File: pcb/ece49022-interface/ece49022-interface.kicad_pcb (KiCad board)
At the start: 4 copper layers, 60.2 x 52.2 mm, 37 parts, among them J1 Conn_01x04_Pin, J2 Conn_01x05_Pin, J3 Conn_01x04_Pin, J4 Conn_01x04_Pin, J5 Conn_01x08_Pin, J6 Conn_01x02_Pin, Q1 KSC1815, U2 TPS54202DDCT

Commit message: added stuff
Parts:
- added J7: Conn_01x04_Pin, Connector_PinHeader_2.54mm:PinHeader_1x04_P2.54mm_Vertical, F.Cu at (137.9, 120.8)
- added J8: Conn_01x04_Pin, Connector_PinHeader_2.54mm:PinHeader_1x04_P2.54mm_Vertical, F.Cu at (137.9, 116.9)
- J5: value Conn_01x08_Pin -> Conn_01x04_Pin; footprint Connector_PinHeader_2.54mm:PinHeader_1x08_P2.54mm_Vertical -> Connector_PinHeader_2.54mm:PinHeader_1x04_P2.54mm_Vertical
- moved J5 15.2 mm to (137.9, 113.0), turned to -90 degrees
- moved H3 12.8 mm to (131.1, 107.4)
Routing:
- net /MAIN_MCU_I2C_SDA: track 36.6 -> 17.6 mm
- net +5V: track 30.2 -> 13.2 mm
- net /MAIN_MCU_I2C_SCL: track 33.8 -> 18.2 mm

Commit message: no warnings
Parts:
- moved Buzzer1 6.68 mm to (141.2, 91.5)
- moved C9 6.68 mm to (183.1, 97.6)
- moved D1 6.68 mm to (180.7, 72.0)
- moved H2 6.68 mm to (189.9, 70.5)
- moved L2 6.68 mm to (181.5, 103.6)
- moved Q1 6.68 mm to (142.9, 100.5)
- moved R1 6.68 mm to (180.9, 85.2)
- moved R10 6.68 mm to (180.9, 96.4)
- moved R14 6.68 mm to (182.9, 92.9)
- moved R5 6.68 mm to (142.2, 77.0)
- moved R9 6.68 mm to (180.9, 94.3)
- moved H4 6.68 mm to (189.8, 116.3)
- moved J1 6.68 mm to (190.8, 81.0)
- moved J6 6.68 mm to (190.8, 92.5)
- moved MOSFET1 6.68 mm to (183.5, 85.3)
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
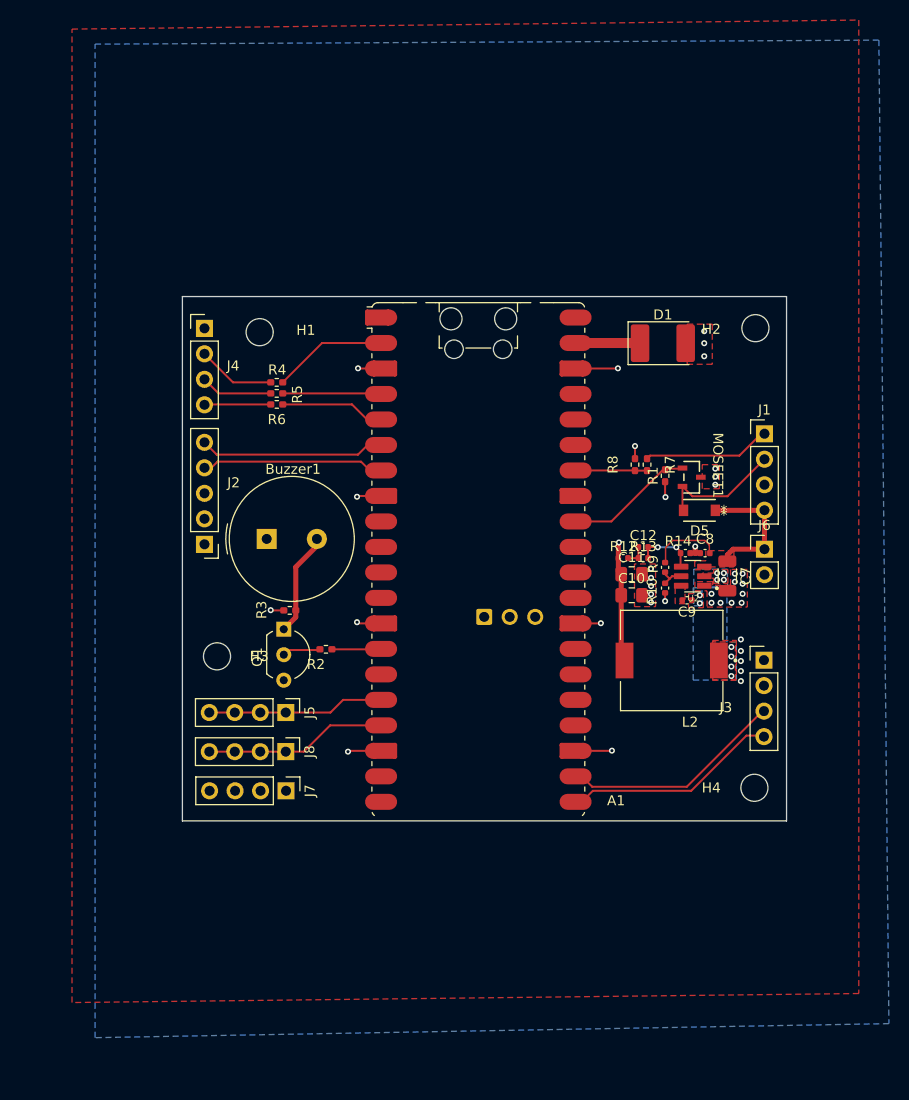
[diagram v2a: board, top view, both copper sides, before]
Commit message: Added cutout
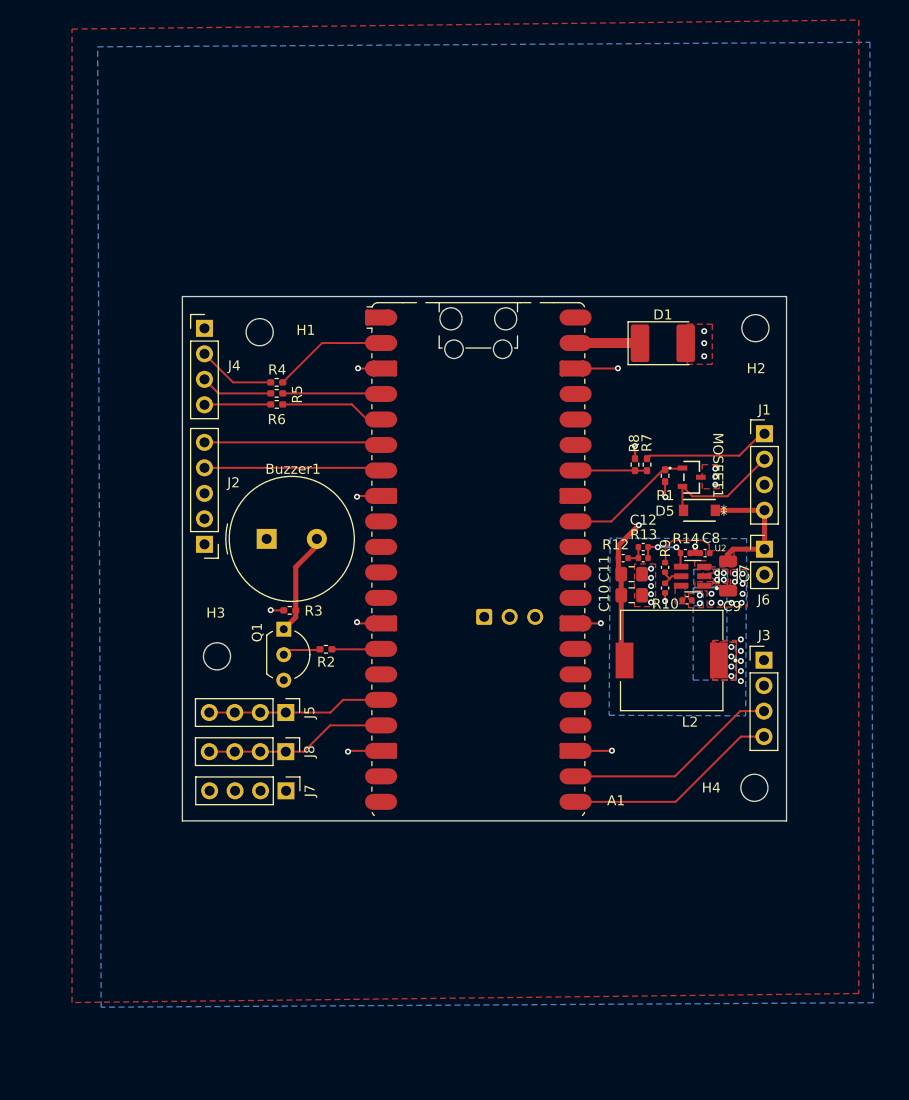
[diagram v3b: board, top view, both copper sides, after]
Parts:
- moved C7 0.08 mm to (187.2, 95.2)
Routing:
- net +5V: track 13.2 -> 15.9 mm
- net /BC_Rx: track 19.1 -> 17.7 mm
- net /BC_Tx: track 18.8 -> 17.7 mm
- net /FS_Rx: track 20.8 -> 21.5 mm
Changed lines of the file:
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@@
 		(tags "capacitor")
 		(property "Reference" "C8"
-			(at 0 1.4 0)
+			(at -0.595 1.492378 0)
 			(layer "F.SilkS")
 			(effects
@@
 		(tags "resistor handsolder")
 		(property "Reference" "R3"
-			(at 2.8025 0.05 90)
+			(at -2.375 -0.0525 0)
 			(layer "F.SilkS")
 			(effects
@@
 		(tags "SMF5V0A-E3-08 ")
 		(property "Reference" "D5"
-			(at -0.011901 -2.0356 0)
+			(at 3.449401 -0.071251 0)
 			(unlocked yes)
 			(layer "F.SilkS")
@@
 		(tags "resistor handsolder")
 		(property "Reference" "R7"
-			(at 0.005 -2.3 90)
+			(at -2.1775 0.025 90)
 			(layer "F.SilkS")
 			(effects
@@
 		(tags "capacitor")
 		(property "Reference" "R10"
-			(at 0.32 1.3 90)
+			(at 1.577622 -0.025 180)
 			(layer "F.SilkS")
 			(effects
@@
 		(tags "Through hole pin header THT 1x02 2.54mm single row")
 		(property "Reference" "J6"
-			(at 0 -2.38 0)
+			(at -0.075 5.05 0)
 			(layer "F.SilkS")
 			(effects
@@
 		(tags "resistor handsolder")
 		(property "Reference" "R8"
-			(at 0 -2.2 90)
+			(at 2.125 -0.075 90)
 			(layer "F.SilkS")
 			(effects
@@
 		(tags "capacitor")
 		(property "Reference" "R9"
-			(at -0.32 1.2 90)
+			(at -1.912378 -0.025 90)
 			(layer "F.SilkS")
 			(effects
@@
 		(tags "TO-92L Inline Wide transistor")
 		(property "Reference" "Q1"
-			(at 2.775 2.65 90)
+			(at 0.3275 2.65 90)
 			(layer "F.SilkS")
 			(effects
@@
 		(at 183.63 95.192378 180)
 		(property "Reference" "U2"
-			(at -0.068 -2.2064 0)
+			(at -2.77 2.792378 0)
 			(layer "F.SilkS")
 			(effects
@@
 	(footprint "Capacitor_SMD:C_1206_3216Metric"
 		(layer "F.Cu")
-		(at 187.075 95.167378 -90)
+		(at 187.15 95.167378 -90)
 		(descr "Capacitor SMD 1206 (3216 Metric), square (rectangular) end terminal, IPC-7351 nominal, (Body size source: IPC-SM-782 page 76, https://www.pcb-3d.com/wordpress/wp-content/uploads/ipc-sm-782a_amendment_1_and_2.pdf), generated with kicad-footprint-generator")
 		(tags "capacitor")
 		(property "Reference" "C7"
-			(at 0 -1.85 90)
+			(at -0.267378 -1.65 270)
 			(layer "F.SilkS")
 			(effects
@@
 		(tags "capacitor")
 		(property "Reference" "R13"
-			(at 0 -1.16 0)
+			(at 0.055 -2.342378 0)
 			(layer "F.SilkS")
 			(effects
@@
 		(tags "capacitor")
 		(property "Reference" "R12"
-			(at 0 -1.16 0)
+			(at -0.745 -1.342378 0)
 			(layer "F.SilkS")
 			(effects
@@
 		(tags "Through hole pin header THT 1x04 2.54mm single row")
 		(property "Reference" "J4"
-			(at 2.85 3.73 0)
+			(at 2.975 3.73 0)
 			(layer "F.SilkS")
 			(effects
@@
 		(tags "capacitor")
 		(property "Reference" "C9"
-			(at 0 -1.16 0)
+			(at -4.495 -0.607622 0)
 			(layer "F.SilkS")
 			(effects
@@
 		(tags "capacitor")
 		(property "Reference" "C12"
-			(at 0 -1.16 0)
+			(at 0.005 -2.692378 0)
 			(layer "F.SilkS")
 			(effects
@@
 		(tags "mountinghole M2.5")
 		(property "Reference" "H3"
-			(at 4.2 0 0)
+			(at -0.125 -4.325 0)
 			(layer "F.SilkS")
 			(effects
@@
 		(tags "mountinghole M2.5")
 		(property "Reference" "H2"
-			(at -4.4 0.1 0)
+			(at 0.075 4.025 0)
 			(layer "F.SilkS")
 			(effects
@@
 		(tags "resistor handsolder")
 		(property "Reference" "R2"
-			(at 0.9975 -1.5 0)
+			(at -0.0225 -1.275 0)
 			(layer "F.SilkS")
 			(effects
@@
 		(tags "Through hole pin header THT 1x04 2.54mm single row")
 		(property "Reference" "J3"
-			(at -3.8 4.72 0)
+			(at 0.025 -2.455 0)
 			(layer "F.SilkS")
 			(effects
@@
 		(tags "capacitor handsolder")
 		(property "Reference" "C11"
-			(at 0 -1.68 0)
+			(at -2.7375 -0.542378 270)
 			(layer "F.SilkS")
 			(effects
@@
 		(tags "capacitor handsolder")
 		(property "Reference" "C10"
-			(at 0 -1.68 0)
+			(at -2.7375 0.307622 90)
 			(layer "F.SilkS")
 			(effects
@@
 		(tags "capacitor")
 		(property "Reference" "R14"
-			(at -0.72 -1.2 0)
+			(at 0.055 -1.442378 0)
 			(layer "F.SilkS")
 			(effects
@@
 		(tags "resistor handsolder")
 		(property "Reference" "R1"
-			(at 0.0025 1.2 90)
+			(at 1.9725 -0.025 180)
 			(layer "F.SilkS")
 			(effects
@@
 	)
 	(segment
-		(start 150.575 83.775)
-		(end 151.455 84.655)
-		(width 0.2)
-		(layer "F.Cu")
-		(net 8)
-	)
-	(segment
 		(start 134.975 84.395)
-		(end 135.655 84.395)
-		(width 0.2)
-		(layer "F.Cu")
-		(net 8)
-	)
-	(segment
-		(start 135.655 84.395)
-		(end 136.275 83.775)
+		(end 152.315 84.395)
 		(width 0.2)
 		(layer "F.Cu")
@@
 	)
 	(segment
-		(start 136.275 83.775)
-		(end 150.575 83.775)
+		(start 152.315 84.395)
+		(end 152.575 84.655)
 		(width 0.2)
 		(layer "F.Cu")
@@
 	)
 	(segment
-		(start 151.455 84.655)
-		(end 153.195 84.655)
-		(width 0.2)
-		(layer "F.Cu")
-		(net 8)
-	)
-	(segment
-		(start 173.615 116.175)
-		(end 183.035 116.175)
+		(start 188.365 108.635)
+		(end 190.725 108.635)
 		(width 0.2)
 		(layer "F.Cu")
@@
 	)
 	(segment
-		(start 172.575 115.135)
-		(end 173.615 116.175)
+		(start 181.865 115.135)
+		(end 188.365 108.635)
 		(width 0.2)
 		(layer "F.Cu")
@@
 	)
 	(segment
-		(start 183.035 116.175)
-		(end 190.675 108.535)
+		(start 171.955 115.135)
+		(end 181.865 115.135)
 		(width 0.2)
 		(layer "F.Cu")
@@
 	)
 	(segment
-		(start 183.475 116.575)
-		(end 188.975 111.075)
+		(start 171.955 117.675)
+		(end 181.925 117.675)
 		(width 0.2)
 		(layer "F.Cu")
@@
 	)
 	(segment
-		(start 188.975 111.075)
-		(end 190.675 111.075)
+		(start 181.925 117.675)
+		(end 188.425 111.175)
 		(width 0.2)
 		(layer "F.Cu")
@@
 	)
 	(segment
-		(start 172.575 117.675)
-		(end 173.675 116.575)
-		(width 0.2)
-		(layer "F.Cu")
-		(net 13)
-	)
-	(segment
-		(start 173.675 116.575)
-		(end 183.475 116.575)
+		(start 188.425 111.175)
+		(end 190.725 111.175)
 		(width 0.2)
 		(layer "F.Cu")
@@
 	(segment
 		(start 134.975 81.855)
-		(end 136.195 83.075)
+		(end 152.315 81.855)
 		(width 0.2)
 		(layer "F.Cu")
@@
 	)
 	(segment
-		(start 150.275 83.075)
-		(end 151.235 82.115)
-		(width 0.2)
-		(layer "F.Cu")
-		(net 14)
-	)
-	(segment
-		(start 151.235 82.115)
-		(end 153.195 82.115)
-		(width 0.2)
-		(layer "F.Cu")
-		(net 14)
-	)
-	(segment
-		(start 136.195 83.075)
-		(end 150.275 83.075)
+		(start 152.315 81.855)
+		(end 152.575 82.115)
 		(width 0.2)
 		(layer "F.Cu")
@@
 	)
 	(segment
-		(start 176.215 93.392378)
-		(end 176.215 91.985)
+		(start 176.215 92.135)
+		(end 178.25 90.1)
 		(width 0.5)
 		(layer "F.Cu")
@@
 		(net 16)
 	)
+	(segment
+		(start 176.215 93.392378)
+		(end 176.215 92.135)
+		(width 0.5)
+		(layer "F.Cu")
+		(net 16)
+	)
 	(via
 		(at 184.775 73.275)
@@
 	)
 	(via
-		(at 176.275 91.825)
+		(at 178.25 90.1)
 		(size 0.6)
 		(drill 0.3)
@@
 	)
 	(zone
-		(net 46)
-		(net_name "Net-(U2-SW)")
+		(net 16)
+		(net_name "+5V")
 		(layer "B.Cu")
 		(hatch edge 0.5)
-		(priority 15)
-		(connect_pads yes
-			(clearance 0.15)
+		(connect_pads thru_hole_only
+			(clearance 0.2)
 		)
 		(min_thickness 0.15)
@@
 			(thermal_gap 0.5)
 			(thermal_bridge_width 0.5)
-			(smoothing fillet)
-			(radius 0.25)
 		)
 		(polygon
 			(pts
-				(xy 183.675 96.342378) (xy 183.675 105.542378) (xy 187.975 105.542378) (xy 187.975 101.742378) (xy 187.035 101.742378)
-				(xy 187.035 96.342378)
+				(xy 201.28 41.99) (xy 201.63 137.69) (xy 124.68 138.14) (xy 124.33 42.44)
+			)
+		)
+		(polygon
+			(pts
+				(xy 175.3 109.05) (xy 188.9 109.1) (xy 189 91.45) (xy 175.4 91.4)
 			)
 		)
 	)
 	(zone
-		(net 16)
-		(net_name "+5V")
+		(net 46)
+		(net_name "Net-(U2-SW)")
 		(layer "B.Cu")
 		(hatch edge 0.5)
-		(priority 2)
-		(connect_pads
-			(clearance 0.5)
+		(priority 15)
+		(connect_pads yes
+			(clearance 0.15)
 		)
-		(min_thickness 0.25)
+		(min_thickness 0.15)
 		(filled_areas_thickness no)
 		(fill yes
 			(thermal_gap 0.5)
 			(thermal_bridge_width 0.5)
+			(smoothing fillet)
+			(radius 0.25)
 		)
 		(polygon
 			(pts
-				(xy 124.075 42.175) (xy 202.175 41.775) (xy 203.175 139.775) (xy 124.075 141.175)
+				(xy 183.675 96.342378) (xy 183.675 105.542378) (xy 187.975 105.542378) (xy 187.975 101.742378) (xy 187.035 101.742378)
+				(xy 187.035 96.342378)
 			)
 		)

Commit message: shelf is ready
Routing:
- net GND: vias 34 -> 32
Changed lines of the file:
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@@
 			(psa4output no)
 			(plot_black_and_white yes)
+			(plotinvisibletext no)
 			(sketchpadsonfab no)
 			(plotpadnumbers no)
@@
 	)
 	(via
-		(at 186.399 97.842378)
-		(size 0.6)
-		(drill 0.3)
-		(layers "F.Cu" "B.Cu")
-		(free yes)
-		(net 3)
-	)
-	(via
 		(at 188.425 104.642378)
 		(size 0.6)
@@
 	)
 	(via
-		(at 187.499 97.842378)
+		(at 186.75 97.8)
 		(size 0.6)
 		(drill 0.3)
@@
 	)
 	(via
-		(at 188.499 97.842378)
-		(size 0.6)
-		(drill 0.3)
-		(layers "F.Cu" "B.Cu")
-		(free yes)
-		(net 3)
-	)
-	(via
-		(at 185.499 97.842378)
+		(at 187.5 97.8)
 		(size 0.6)
 		(drill 0.3)
@@
 	)
 	(via
-		(at 188.599 96.942378)
+		(at 188.525 96.942378)
 		(size 0.6)
 		(drill 0.3)
@@
 	)
 	(via
-		(at 185.499 96.942378)
-		(size 0.6)
-		(drill 0.3)
-		(layers "F.Cu" "B.Cu")
-		(free yes)
-		(net 3)
-	)
-	(via
 		(at 188.425 105.642378)
 		(size 0.6)
@@
 	)
 	(via
-		(at 188.599 95.942378)
+		(at 188.599 95.725)
 		(size 0.6)
 		(drill 0.3)
@@
 		(net 3)
 	)
+	(via
+		(at 188.325 97.8)
+		(size 0.6)
+		(drill 0.3)
+		(layers "F.Cu" "B.Cu")
+		(free yes)
+		(net 3)
+	)
 	(segment
 		(start 178.355 71.955)
@@
 	)
 	(via
-		(at 184.3325 97.892378)
+		(at 184.325 97.775)
 		(size 0.6)
 		(drill 0.3)
@@
 		(polygon
 			(pts
-				(xy 183.7266 98.131978) (xy 184.5522 98.131978) (xy 184.5522 96.253978) (xy 187.087 96.253978) (xy 187.087 94.492378)
+				(xy 183.7266 98.131978) (xy 184.7522 98.131978) (xy 184.7522 96.253978) (xy 187.087 96.253978) (xy 187.087 94.492378)
 				(xy 183.727988 94.492378)
 			)
@@
 		(polygon
 			(pts
-				(xy 183.675 96.342378) (xy 183.675 105.542378) (xy 187.975 105.542378) (xy 187.975 101.742378) (xy 187.035 101.742378)
-				(xy 187.035 96.342378)
+				(xy 183.725 96.242378) (xy 183.725 105.542378) (xy 187.975 105.542378) (xy 187.975 96.242378)
 			)
 		)

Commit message: breakout pins
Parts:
- added J9: Conn_01x05_Pin, Connector_PinHeader_2.54mm:PinHeader_1x05_P2.54mm_Vertical, F.Cu at (147.8, 89.8)
- moved J2 11.3 mm to (137.8, 81.0), turned to 90 degrees
- moved R3 5.09 mm to (139.1, 101.2), turned to -90 degrees
- moved R2 2.49 mm to (146.8, 105.0)
- moved Buzzer1 2.15 mm to (139.4, 90.2), turned to -90 degrees
- moved Q1 0.95 mm to (141.9, 100.7)
- moved J4 0.89 mm to (135.1, 69.6)
- moved R4 0.78 mm to (142.2, 75.1)
- moved R6 0.78 mm to (142.2, 77.3)
- moved R5 0.77 mm to (142.2, 76.2)
- moved H3 0.71 mm to (136.0, 103.8)
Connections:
- A1 pad 10: unconnected-(A1-GPIO7-Pad10) -> Net-(A1-GPIO7)
- A1 pad 11: unconnected-(A1-GPIO8-Pad11) -> Net-(A1-GPIO8)
- A1 pad 12: unconnected-(A1-GPIO9-Pad12) -> Net-(A1-GPIO9)
- A1 pad 14: /GPIO10 -> Net-(A1-GPIO10)
- A1 pad 15: unconnected-(A1-GPIO11-Pad15) -> /GPIO11
- A1 pad 24: unconnected-(A1-GPIO18-Pad24) -> Net-(A1-GPIO18)
- A1 pad 25: unconnected-(A1-GPIO19-Pad25) -> Net-(A1-GPIO19)
- A1 pad 26: unconnected-(A1-GPIO20-Pad26) -> Net-(A1-GPIO20)
- A1 pad 27: unconnected-(A1-GPIO21-Pad27) -> Net-(A1-GPIO21)
- A1 pad 29: unconnected-(A1-GPIO22-Pad29) -> Net-(A1-GPIO22)
- A1 pad 31: unconnected-(A1-GPIO26_ADC0-Pad31) -> Net-(A1-GPIO26_ADC0)
- A1 pad 9: unconnected-(A1-GPIO6-Pad9) -> Net-(A1-GPIO6)
- R2 pad 1: /GPIO10 -> /GPIO11
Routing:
- net /BC_Rx: track 17.7 -> 5.04 mm
- net Net-(A1-GPIO10): track 0.00 -> 7.30 mm
- net /BC_Tx: track 17.7 -> 10.7 mm
- net /GPIO10: track 5.54 -> 0.00 mm
- net /GPIO11: track 0.00 -> 5.19 mm
- net Net-(A1-GPIO9): track 0.00 -> 4.83 mm
- net Net-(A1-GPIO8): track 0.00 -> 4.83 mm
- net Net-(A1-GPIO7): track 0.00 -> 4.83 mm
- net Net-(A1-GPIO6): track 0.00 -> 4.83 mm
- net Net-(Q1-C): track 10.7 -> 8.43 mm
- net Net-(Q1-B): track 3.79 -> 5.18 mm

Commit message: update
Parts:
- removed J9: Conn_01x05_Pin, Connector_PinHeader_2.54mm:PinHeader_1x05_P2.54mm_Vertical
- added J10: Conn_01x06_Pin, Connector_PinHeader_2.54mm:PinHeader_1x06_P2.54mm_Vertical, F.Cu at (148.0, 89.8)
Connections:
- A1 pad 10: Net-(A1-GPIO7) -> /GPIO7
- A1 pad 11: Net-(A1-GPIO8) -> /GPIO8
- A1 pad 12: Net-(A1-GPIO9) -> /GPIO9
- A1 pad 14: Net-(A1-GPIO10) -> /GPIO10
- A1 pad 24: Net-(A1-GPIO18) -> unconnected-(A1-GPIO18-Pad24)
- A1 pad 25: Net-(A1-GPIO19) -> unconnected-(A1-GPIO19-Pad25)
- A1 pad 26: Net-(A1-GPIO20) -> unconnected-(A1-GPIO20-Pad26)
- A1 pad 27: Net-(A1-GPIO21) -> unconnected-(A1-GPIO21-Pad27)
- A1 pad 29: Net-(A1-GPIO22) -> unconnected-(A1-GPIO22-Pad29)
- A1 pad 31: Net-(A1-GPIO26_ADC0) -> unconnected-(A1-GPIO26_ADC0-Pad31)
- A1 pad 9: Net-(A1-GPIO6) -> /GPIO6
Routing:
- net Net-(A1-GPIO10): track 7.30 -> 0.00 mm
- net Net-(A1-GPIO9): track 4.83 -> 0.00 mm
- net Net-(A1-GPIO8): track 4.83 -> 0.00 mm
- net Net-(A1-GPIO7): track 4.83 -> 0.00 mm
- net Net-(A1-GPIO6): track 4.83 -> 0.00 mm
- net /GPIO9: track 0.00 -> 4.58 mm
- net /GPIO8: track 0.00 -> 4.58 mm
- net /GPIO7: track 0.00 -> 4.58 mm
- net /GPIO6: track 0.00 -> 4.58 mm
- net /GPIO10: track 0.00 -> 4.58 mm
- net GND: track 27.4 -> 28.9 mm, vias 32 -> 31
